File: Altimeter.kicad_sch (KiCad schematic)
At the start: 46 parts, among them U1 ESP32-S3, Y1 40MHz±10ppm

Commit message: 2nd iteration to be reviewed
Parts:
- removed 12VLED1: 12V_LED, Resistor_SMD:R_0402_1005Metric, symbol Device:LED_Small
- removed 27Ω, 47Ω: R, symbol Device:R
- removed J?: Conn_01x03_Male, Connector_PinHeader_2.54mm:PinHeader_1x03_P2.54mm_Vertical, symbol Connector:Conn_01x03_Male
- removed J?: Conn_01x04_Male, symbol Connector:Conn_01x04_Male
- removed R4: 3k, Resistor_SMD:R_0402_1005Metric, symbol Device:R_Small
- removed R? (x2): 4.7k, symbol Device:R_Small
- removed RXLED1: RX_LED, LED_SMD:LED_0603_1608Metric, symbol Device:LED_Small
- removed U?: LTST-FS63HBGED, symbol Custom_Components:LTST-FS63HBGED
- removed U?: W25N04KVxxIRU, symbol Custom_Components:W25N04KVxxIRU
- added C40: 10uF, Capacitor_SMD:C_0402_1005Metric, symbol Device:C_Small
- added IC1: XTSD02GLGEAG, iclr:SOTFL50P160X60-8N, symbol chest:XTSD08GLGEAG
- added J1: Conn_01x04_Male, Connector_PinHeader_2.54mm:PinHeader_1x04_P2.54mm_Vertical, symbol Connector:Conn_01x04_Male
- added J2: Conn_01x02_Male, Connector_JST:JST_PH_B2B-PH-K_1x02_P2.00mm_Vertical, symbol Connector:Conn_01x02_Male
- added Q1: PMV20ENR, Package_TO_SOT_SMD:SOT-23, symbol Device:Q_NMOS_GSD
- added R5: 309, Resistor_SMD:R_0402_1005Metric, symbol Device:R
- added R6: 30, Resistor_SMD:R_0402_1005Metric, symbol Device:R
- added R7: 158, Resistor_SMD:R_0402_1005Metric, symbol Device:R
- added R9: 499, Resistor_SMD:R_0402_1005Metric, symbol Device:R
- added TP1, TP10, TP11, TP12, TP13, TP14, TP15, TP2: TestPoint, TestPoint:TestPoint_Pad_D1.0mm, symbol Connector:TestPoint
- added U1: 150044M155220, iclr:150044M155220, symbol iclr:150044M155220
- C1: renamed from C4; footprint (none) -> Capacitor_SMD:C_0402_1005Metric
- C12: value C -> 4.2pF
- C13, C14: footprint Capacitor_SMD:C_0603_1608Metric -> Capacitor_SMD:C_0402_1005Metric
- C15, C16: renamed from C?; footprint Capacitor_SMD:C_0603_1608Metric -> Capacitor_SMD:C_0402_1005Metric
- L1, L2: footprint (none) -> Inductor_SMD:L_0402_1005Metric
- R10: value 470 -> 1k
- R8: renamed from R1; value 50 -> 47.5; footprint (none) -> Resistor_SMD:R_0402_1005Metric
- U2: renamed from U1; footprint Package_DFN_QFN:QFN-56-1EP_7x7mm_P0.4mm_EP5.6x5.6mm -> iclr:QFN40P700X700X90-57N
- U4: renamed from U?; footprint XDCR_DPS310 -> iclr:XDCR_DPS310
- renumbered C3 to C10, C1 to C3, C5 to C4, C6 to C5, C7 to C6, C8 to C7, C9 to C8, C10 to C9, R7 to R1, R11 to R2, R8 to R3, R14 to R4
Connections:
- net +3V3: now also C40.1, J2.2 (Pin_2)
- net BattVolt: now also U2.15 (GPIO10/ADC1_CH9)
- net GND: now also IC1.4 (GND), J1.1 (Pin_1), J1.3 (Pin_3), Q1.2 (S)
- net MISO: now also U2.37 (SPICLK_P/GPIO47), TP12.1; no longer U2.12 (GPIO7/ADC1_CH6)
- net MOSI: now also U2.38 (GPIO33), TP10.1; no longer U2.11 (GPIO6/ADC1_CH5)
- net RXD: now also U2.47 (MTDI/JTAG/GPIO41), TP2.1
- net SCLK: now also U2.39 (GPIO34), TP11.1
- net TXD: now also R9.1, TP1.1
- net at R10.2: now also J2.1 (Pin_1), Q1.3 (D)
- net at U2.27 (GPIO21): now also U4.2 (~{CSB})
- net at U2.40 (GPIO35): now also J1.4 (Pin_4); no longer U4.2 (~{CSB})
- net at U2.16 (GPIO11/ADC2_CH0): now also IC1.5 (CMD/DI)
- net at U2.17 (GPIO12/ADC2_CH1): now also IC1.6 (SD0/DO), TP14.1
- net at U2.18 (GPIO13/ADC2_CH2): now also IC1.3 (CLK), TP13.1
- net at U2.19 (GPIO14/ADC2_CH3): now also IC1.2 (SD3/CS), TP15.1
- net IMU/Magnetometer: now reaches U2.24 (GPIO18/ADC2_CH7/DAC_1)
- net Accel/Gyro: now reaches U2.44 (MTCK/JTAG/GPIO39)
- net at U2.48 (MTMS/JTAG/GPIO42): now also R9.2
- net at U2.6 (GPIO1/ADC1_CH0): now also R5.2
- net at U2.7 (GPIO2/ADC1_CH1): now also R6.2
- net IMU/CSAccel renamed IMU/Accelerometer
- net IMU/CSAccel/Gyro renamed Buzzer
- net Buzzer: now also Q1.1 (G)
- net IMU/CSMag: no longer names the net of U2.41 (GPIO36)
- net IMU/CSMag: now also J1.2 (Pin_2)
- net SCL: no longer names the net of U2.9 (GPIO4/ADC1_CH3)
- net SCL: now also R7.2
- net SDA: no longer names the net of U2.10 (GPIO5/ADC1_CH4)
- new net: C40.2, IC1.8 (VDD)
- new net: R5.1, U1.2 (R)
- new net: R6.1, U1.3 (B)
- new net: R7.1, U1.4 (G)
- new net +3.3V: U1.1 (V)
- no-connect marks 12 -> 25
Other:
- removed sheet CAN-BUS
- sheet IMU ports: added Accelerometer, Accel/Gyro, Magnetometer; removed CSAccel, CSAccel/Gyro, CSMag
- note removed: "CAN + is CAN High CAN - is CAN LOW Named with a + and - as it is a KiCad requirement to route differential tracks"
- note removed: "TBD C and R value to get a total series impedance of 50 ohms at 2.4GHz"
- note removed: "might need checking and footprint"
- moved on the sheet: C10, R2, TXLED1

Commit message: 3rd iteration
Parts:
- added TP7: TestPoint, TestPoint:TestPoint_Pad_D1.0mm, symbol Connector:TestPoint
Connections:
- net +3V3: now also IC1.8 (VDD)
- net GND: now also C40.2
- net at IC1.5 (CMD/DI), U2.16 (GPIO11/ADC2_CH0): now also TP7.1
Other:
- moved on the sheet: C40
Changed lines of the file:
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@@
   (junction (at 34.29 167.64) (diameter 0) (color 0 0 0 0)
   )
+  (junction (at 43.18 96.52) (diameter 0) (color 0 0 0 0)
+  )
   (junction (at 16.51 101.6) (diameter 0) (color 0 0 0 0)
   )
@@
   )
   (junction (at 45.72 170.18) (diameter 0) (color 0 0 0 0)
+  )
+  (junction (at 60.96 97.79) (diameter 0) (color 0 0 0 0)
   )
   (junction (at 29.21 135.89) (diameter 0) (color 0 0 0 0)
@@
     (stroke (width 0) (type default))
   )
-  (wire (pts (xy 44.45 100.33) (xy 46.99 100.33))
-    (stroke (width 0) (type default))
-  )
   (wire (pts (xy 210.82 111.76) (xy 210.82 93.98))
     (stroke (width 0) (type default))
@@
     (stroke (width 0) (type default))
   )
-  (wire (pts (xy 44.45 99.06) (xy 43.18 99.06))
-    (stroke (width 0) (type default))
-  )
   (wire (pts (xy 34.29 67.31) (xy 31.75 67.31))
     (stroke (width 0) (type default))
@@
     (stroke (width 0) (type default))
   )
-  (wire (pts (xy 44.45 99.06) (xy 44.45 100.33))
-    (stroke (width 0) (type default))
-  )
   (wire (pts (xy 54.61 102.87) (xy 69.85 102.87))
     (stroke (width 0) (type default))
@@
     (stroke (width 0) (type default))
   )
+  (wire (pts (xy 43.18 99.06) (xy 43.18 96.52))
+    (stroke (width 0) (type default))
+  )
   (polyline (pts (xy 124.46 111.76) (xy 124.46 114.3))
     (stroke (width 0) (type default))
   )
-  (wire (pts (xy 46.99 95.25) (xy 43.18 95.25))
-    (stroke (width 0) (type default))
-  )
-  (wire (pts (xy 52.07 97.79) (xy 69.85 97.79))
+  (wire (pts (xy 52.07 97.79) (xy 60.96 97.79))
     (stroke (width 0) (type default))
   )
@@
     (stroke (width 0) (type default))
   )
+  (wire (pts (xy 60.96 97.79) (xy 69.85 97.79))
+    (stroke (width 0) (type default))
+  )
   (polyline (pts (xy 90.17 76.2) (xy 90.17 78.74))
     (stroke (width 0) (type default))
@@
     (stroke (width 0) (type default))
   )
+  (wire (pts (xy 60.96 96.52) (xy 60.96 97.79))
+    (stroke (width 0) (type default))
+  )
   (wire (pts (xy 16.51 114.3) (xy 43.18 114.3))
     (stroke (width 0) (type default))
@@
   )
   (wire (pts (xy 201.93 124.46) (xy 201.93 125.73))
+    (stroke (width 0) (type default))
+  )
+  (wire (pts (xy 43.18 96.52) (xy 43.18 95.25))
     (stroke (width 0) (type default))
   )
@@
     )
   )
-  (symbol (lib_id "Device:C_Small") (at 46.99 97.79 0) (unit 1)
-    (in_bom yes) (on_board yes) (dnp no)
-    (property "Reference" "C40" (at 40.64 96.52 0)
-      (effects (font (size 1.27 1.27)) (justify left))
-    )
-    (property "Value" "10uF" (at 44.45 101.6 0)
-      (effects (font (size 1.27 1.27)) (justify left))
-    )
-    (property "Footprint" "Capacitor_SMD:C_0402_1005Metric" (at 46.99 97.79 0)
-      (effects (font (size 1.27 1.27)) hide)
-    )
-    (property "Datasheet" "~" (at 46.99 97.79 0)
+  (symbol (lib_id "Device:C_Small") (at 45.72 96.52 90) (unit 1)
+    (in_bom yes) (on_board yes) (dnp no)
+    (property "Reference" "C40" (at 48.26 91.44 90)
+      (effects (font (size 1.27 1.27)) (justify left))
+    )
+    (property "Value" "10uF" (at 49.53 93.98 90)
+      (effects (font (size 1.27 1.27)) (justify left))
+    )
+    (property "Footprint" "Capacitor_SMD:C_0402_1005Metric" (at 45.72 96.52 0)
+      (effects (font (size 1.27 1.27)) hide)
+    )
+    (property "Datasheet" "~" (at 45.72 96.52 0)
       (effects (font (size 1.27 1.27)) hide)
     )
@@
         (path "/7db990e4-92e1-4f99-b4d2-435bbec1ba83"
           (reference "C15") (unit 1)
+        )
+      )
+    )
+  )
+  (symbol (lib_id "power:GND") (at 48.26 96.52 0) (unit 1)
+    (in_bom yes) (on_board yes) (dnp no)
+    (property "Reference" "#PWR025" (at 48.26 102.87 0)
+      (effects (font (size 1.27 1.27)) hide)
+    )
+    (property "Value" "GND" (at 46.99 100.33 0)
+      (effects (font (size 1.27 1.27)))
+    )
+    (property "Footprint" "" (at 48.26 96.52 0)
+      (effects (font (size 1.27 1.27)) hide)
+    )
+    (property "Datasheet" "" (at 48.26 96.52 0)
+      (effects (font (size 1.27 1.27)) hide)
+    )
+    (pin "1")
+    (instances
+      (project "Altimeter"
+        (path "/7db990e4-92e1-4f99-b4d2-435bbec1ba83"
+          (reference "#PWR025") (unit 1)
         )
       )
@@
         (path "/7db990e4-92e1-4f99-b4d2-435bbec1ba83"
           (reference "TP13") (unit 1)
+        )
+      )
+    )
+  )
+  (symbol (lib_id "Connector:TestPoint") (at 60.96 96.52 0) (unit 1)
+    (in_bom yes) (on_board yes) (dnp no)
+    (property "Reference" "TP7" (at 62.23 90.17 0)
+      (effects (font (size 1.27 1.27)) (justify right))
+    )
+    (property "Value" "TestPoint" (at 64.77 87.63 0)
+      (effects (font (size 1.27 1.27)) (justify right))
+    )
+    (property "Footprint" "TestPoint:TestPoint_Pad_D1.0mm" (at 66.04 96.52 0)
+      (effects (font (size 1.27 1.27)) hide)
+    )
+    (property "Datasheet" "~" (at 66.04 96.52 0)
+      (effects (font (size 1.27 1.27)) hide)
+    )
+    (pin "1")
+    (instances
+      (project "Altimeter"
+        (path "/7db990e4-92e1-4f99-b4d2-435bbec1ba83"
+          (reference "TP7") (unit 1)
         )
       )
@@
   (symbol (lib_id "Connector:TestPoint") (at 50.8 100.33 0) (unit 1)
     (in_bom yes) (on_board yes) (dnp no)
-    (property "Reference" "TP14" (at 53.34 91.44 0)
+    (property "Reference" "TP14" (at 55.88 95.25 0)
       (effects (font (size 1.27 1.27)) (justify right))
     )
-    (property "Value" "TestPoint" (at 55.88 88.9 0)
+    (property "Value" "TestPoint" (at 58.42 92.71 0)
       (effects (font (size 1.27 1.27)) (justify right))
     )

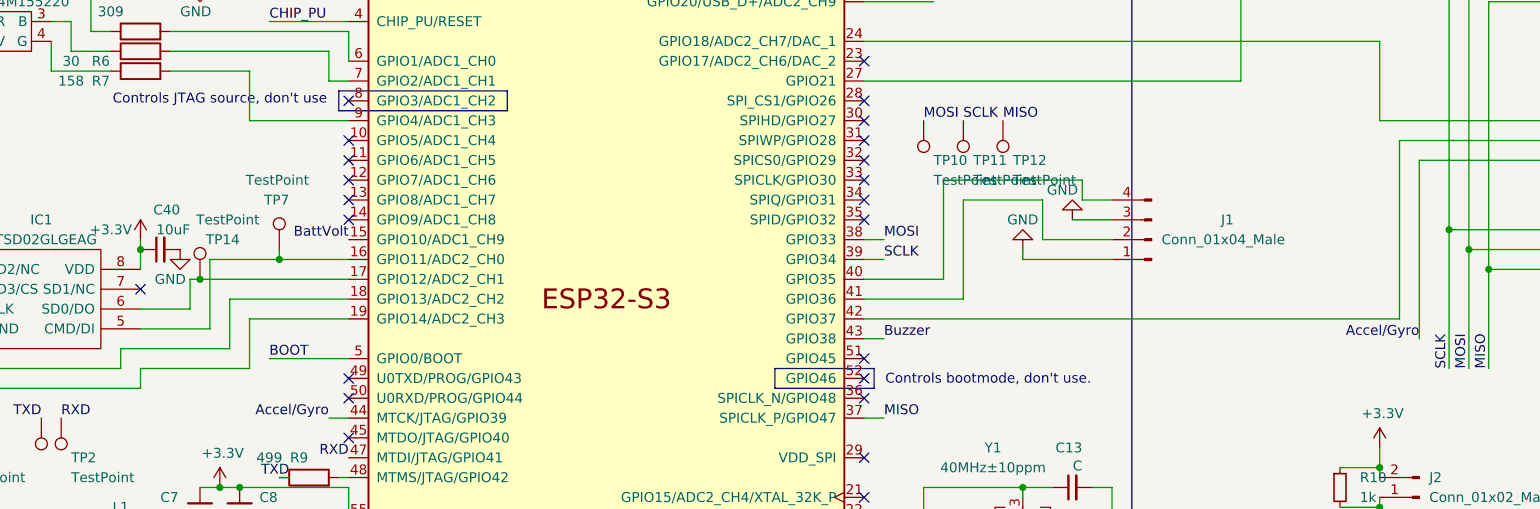
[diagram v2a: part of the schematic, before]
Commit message: 3rd iteration with new tracer spacing of 0.15
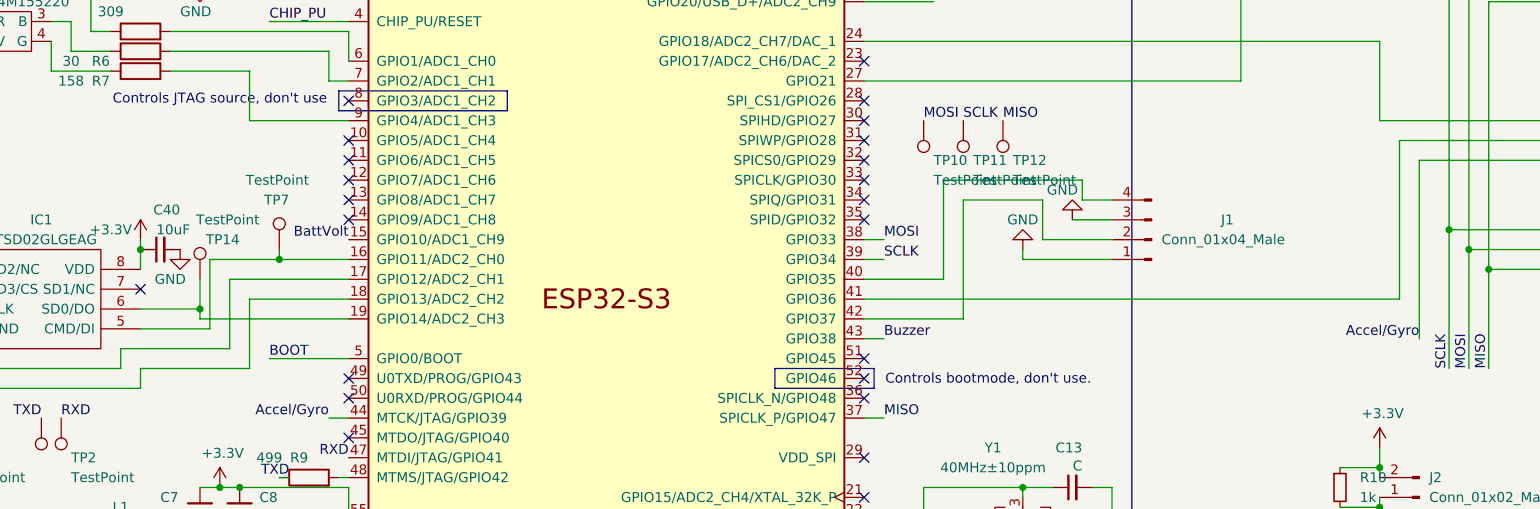
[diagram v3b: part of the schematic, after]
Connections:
- net IMU/Accelerometer: now also U2.41 (GPIO36); no longer U2.42 (GPIO37)
- net at IC1.2 (SD3/CS), TP15.1: now also U2.18 (GPIO13/ADC2_CH2); no longer U2.19 (GPIO14/ADC2_CH3)
- net at IC1.3 (CLK), TP13.1: now also U2.17 (GPIO12/ADC2_CH1); no longer U2.18 (GPIO13/ADC2_CH2)
- net at IC1.6 (SD0/DO), TP14.1: now also U2.19 (GPIO14/ADC2_CH3); no longer U2.17 (GPIO12/ADC2_CH1)
- net at J1.2 (Pin_2): now also U2.42 (GPIO37); no longer U2.41 (GPIO36)
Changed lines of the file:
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@@
   (junction (at 210.82 93.98) (diameter 0) (color 0 0 0 0)
   )
+  (junction (at 50.8 104.14) (diameter 0) (color 0 0 0 0)
+  )
   (junction (at 69.85 142.24) (diameter 0) (color 0 0 0 0)
   )
@@
   )
   (junction (at 34.29 135.89) (diameter 0) (color 0 0 0 0)
-  )
-  (junction (at 50.8 100.33) (diameter 0) (color 0 0 0 0)
   )
   (junction (at 20.32 135.89) (diameter 0) (color 0 0 0 0)
@@
     (stroke (width 0) (type default))
   )
-  (wire (pts (xy 50.8 100.33) (xy 69.85 100.33))
-    (stroke (width 0) (type default))
-  )
   (polyline (pts (xy 90.17 78.74) (xy 68.58 78.74))
     (stroke (width 0) (type default))
@@
     (stroke (width 0) (type default))
   )
+  (wire (pts (xy 50.8 105.41) (xy 69.85 105.41))
+    (stroke (width 0) (type default))
+  )
   (wire (pts (xy 16.51 191.77) (xy 20.32 191.77))
     (stroke (width 0) (type default))
@@
     (stroke (width 0) (type default))
   )
-  (wire (pts (xy 57.15 105.41) (xy 69.85 105.41))
+  (wire (pts (xy 57.15 102.87) (xy 69.85 102.87))
     (stroke (width 0) (type default))
   )
@@
     (stroke (width 0) (type default))
   )
+  (wire (pts (xy 50.8 104.14) (xy 50.8 105.41))
+    (stroke (width 0) (type default))
+  )
   (wire (pts (xy 16.51 170.18) (xy 16.51 171.45))
     (stroke (width 0) (type default))
@@
     (stroke (width 0) (type default))
   )
-  (wire (pts (xy 49.53 100.33) (xy 50.8 100.33))
-    (stroke (width 0) (type default))
-  )
-  (wire (pts (xy 135.89 105.41) (xy 204.47 105.41))
-    (stroke (width 0) (type default))
-  )
-  (wire (pts (xy 43.18 104.14) (xy 49.53 104.14))
+  (wire (pts (xy 135.89 102.87) (xy 204.47 102.87))
+    (stroke (width 0) (type default))
+  )
+  (wire (pts (xy 43.18 104.14) (xy 50.8 104.14))
     (stroke (width 0) (type default))
   )
@@
     (stroke (width 0) (type default))
   )
-  (wire (pts (xy 204.47 82.55) (xy 204.47 105.41))
+  (wire (pts (xy 204.47 82.55) (xy 204.47 102.87))
     (stroke (width 0) (type default))
   )
@@
     (stroke (width 0) (type default))
   )
-  (wire (pts (xy 54.61 102.87) (xy 69.85 102.87))
-    (stroke (width 0) (type default))
-  )
   (wire (pts (xy 156.21 127) (xy 156.21 128.27))
     (stroke (width 0) (type default))
@@
     (stroke (width 0) (type default))
   )
-  (wire (pts (xy 49.53 100.33) (xy 49.53 104.14))
-    (stroke (width 0) (type default))
-  )
   (wire (pts (xy 271.78 44.45) (xy 271.78 41.91))
     (stroke (width 0) (type default))
@@
     (stroke (width 0) (type default))
   )
-  (wire (pts (xy 57.15 111.76) (xy 57.15 105.41))
+  (wire (pts (xy 57.15 111.76) (xy 57.15 102.87))
     (stroke (width 0) (type default))
   )
@@
     (stroke (width 0) (type default))
   )
-  (wire (pts (xy 148.59 90.17) (xy 148.59 102.87))
+  (wire (pts (xy 148.59 90.17) (xy 148.59 105.41))
     (stroke (width 0) (type default))
   )
@@
     (stroke (width 0) (type default))
   )
-  (wire (pts (xy 54.61 102.87) (xy 54.61 109.22))
+  (wire (pts (xy 54.61 100.33) (xy 54.61 109.22))
     (stroke (width 0) (type default))
   )
@@
     (stroke (width 0) (type default))
   )
+  (wire (pts (xy 54.61 100.33) (xy 69.85 100.33))
+    (stroke (width 0) (type default))
+  )
   (wire (pts (xy 156.21 97.79) (xy 167.64 97.79))
     (stroke (width 0) (type default))
@@
     (stroke (width 0) (type default))
   )
-  (wire (pts (xy 148.59 102.87) (xy 135.89 102.87))
+  (wire (pts (xy 148.59 105.41) (xy 135.89 105.41))
     (stroke (width 0) (type default))
   )
@@
     (stroke (width 0) (type default))
   )
+  (wire (pts (xy 50.8 100.33) (xy 50.8 104.14))
+    (stroke (width 0) (type default))
+  )

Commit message: hopefully final commit
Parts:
- C12: footprint Capacitor_SMD:C_0603_1608Metric -> Capacitor_SMD:C_0402_1005Metric
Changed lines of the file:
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@@
       (effects (font (size 1.27 1.27)) (justify left))
     )
-    (property "Footprint" "Capacitor_SMD:C_0603_1608Metric" (at 66.04 62.23 0)
+    (property "Footprint" "Capacitor_SMD:C_0402_1005Metric" (at 66.04 62.23 0)
       (effects (font (size 1.27 1.27)) hide)
     )
